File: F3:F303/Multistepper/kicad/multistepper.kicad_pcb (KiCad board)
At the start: 4 copper layers, 113.5 x 105.5 mm, 231 parts, among them J1 Prog, J10 Screw_Terminal_01x02, J11 LimS, J12 Stepper, J13 UART, J14 LimS, J15 Stepper, J16 LimS, J17 Stepper, J18 LimS, J19 Stepper, J2 Buttons/I2C, J20 LimS, J21 Stepper, J22 LimS, J23 Stepper, J24 LimS, J25 Stepper, J26 LimS, J27 Stepper, J3 Screen, J4 ADC2, J5 ADC1, J6 MOT_MUL, J7 GPO, J8 USB_B, J9 Screw_Terminal_01x03, Q1 B0505S, Q2 IRF9310, SW1 Reset, SW2 Boot, SW3 SW_DIP_x01, U1 STM32F303VDTx, U2 ISO1050DUB, U3 USBLC6-2SC6, U4 LM4050A(b)EX3-3.3, U5 LM2576-5.0, U6 LM1117-3.3, U7 74HC4051, Y1 NX5032GA-8MHz

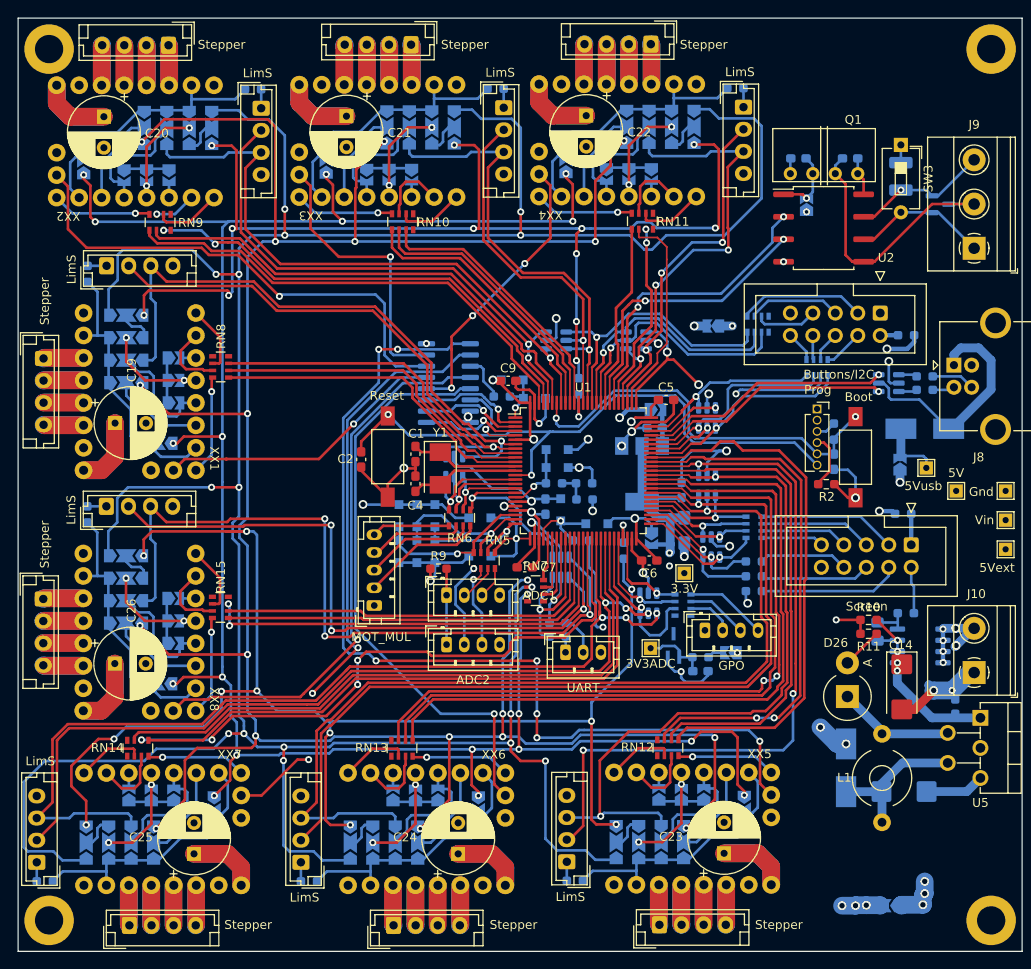
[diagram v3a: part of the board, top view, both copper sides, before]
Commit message: Multistepper PCB almost ready
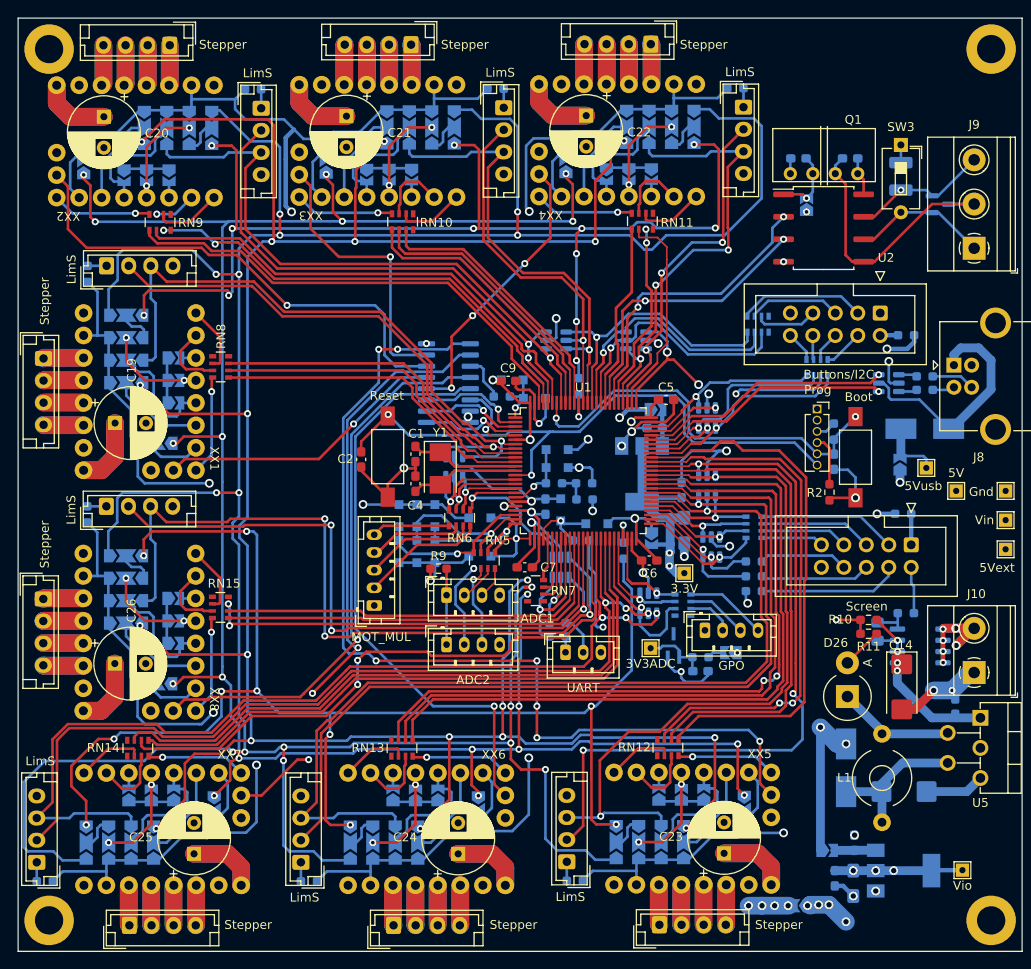
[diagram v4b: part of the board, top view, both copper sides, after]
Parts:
- added C27: 0.1, Capacitor_SMD:C_0603_1608Metric_Pad1.08x0.95mm_HandSolder, B.Cu at (150.0, 131.7)
- added C28: 47u 6V, Capacitor_Tantalum_SMD:CP_EIA-3216-18_Kemet-A_Pad1.58x1.35mm_HandSolder, B.Cu at (149.9, 136.3)
- added C29: 0.1, Capacitor_SMD:C_0603_1608Metric_Pad1.08x0.95mm_HandSolder, B.Cu at (147.8, 135.7)
- added TP8: Vio, TestPoint:TestPoint_THTPad_1.5x1.5mm_Drill0.7mm, F.Cu at (162.3, 134.8)
- added U8: LM1117-3.3, Package_TO_SOT_SMD:SOT-223-3_TabPin2, B.Cu at (155.6, 134.9)
- moved JP7 60.7 mm to (147.0, 132.6), turned to 0 degrees
- moved JP6 10.3 mm to (144.0, 138.8)
- moved R2 0.98 mm to (147.2, 92.1), turned to 90 degrees
- moved J15 0.14 mm to (72.6, 41.6)
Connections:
- JP10 pad 3: /Motors/Vio -> Vio
- JP11 pad 3: /Motors/Vio -> Vio
- JP12 pad 3: /Motors/Vio -> Vio
- JP16 pad 3: /Motors/Vio -> Vio
- JP18 pad 3: /Motors/Vio -> Vio
- JP19 pad 3: /Motors/Vio -> Vio
- JP20 pad 3: /Motors/Vio -> Vio
- JP24 pad 3: /Motors/Vio -> Vio
- JP26 pad 3: /Motors/Vio -> Vio
- JP27 pad 3: /Motors/Vio -> Vio
- JP28 pad 3: /Motors/Vio -> Vio
- JP32 pad 3: /Motors/Vio -> Vio
- JP34 pad 3: /Motors/Vio -> Vio
- JP35 pad 3: /Motors/Vio -> Vio
- JP36 pad 3: /Motors/Vio -> Vio
- JP40 pad 3: /Motors/Vio -> Vio
- JP42 pad 3: /Motors/Vio -> Vio
- JP43 pad 3: /Motors/Vio -> Vio
- JP44 pad 3: /Motors/Vio -> Vio
- JP48 pad 3: /Motors/Vio -> Vio
- JP50 pad 3: /Motors/Vio -> Vio
- JP51 pad 3: /Motors/Vio -> Vio
- JP52 pad 3: /Motors/Vio -> Vio
- JP56 pad 3: /Motors/Vio -> Vio
- JP58 pad 3: /Motors/Vio -> Vio
- JP59 pad 3: /Motors/Vio -> Vio
- JP60 pad 3: /Motors/Vio -> Vio
- JP64 pad 3: /Motors/Vio -> Vio
- JP66 pad 3: /Motors/Vio -> Vio
- JP67 pad 3: /Motors/Vio -> Vio
- JP68 pad 3: /Motors/Vio -> Vio
- JP7 pad 1: +3V3 -> +5V
- JP7 pad 2: /Motors/Vio -> Net-(C27-Pad1)
- JP8 pad 3: /Motors/Vio -> Vio
- R23 pad 1: /Motors/Vio -> Vio
- R26 pad 1: /Motors/Vio -> Vio
- R27 pad 1: /Motors/Vio -> Vio
- R28 pad 1: /Motors/Vio -> Vio
- R29 pad 1: /Motors/Vio -> Vio
- R30 pad 1: /Motors/Vio -> Vio
- R31 pad 1: /Motors/Vio -> Vio
- R32 pad 1: /Motors/Vio -> Vio
- U7 pad 16: /Motors/Vio -> Vio
- XX1 pad 10: /Motors/Vio -> Vio
- XX2 pad 10: /Motors/Vio -> Vio
- XX3 pad 10: /Motors/Vio -> Vio
- XX4 pad 10: /Motors/Vio -> Vio
- XX5 pad 10: /Motors/Vio -> Vio
- XX6 pad 10: /Motors/Vio -> Vio
- XX7 pad 10: /Motors/Vio -> Vio
- XX8 pad 10: /Motors/Vio -> Vio
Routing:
- net /Motors/Vio: track 587.4 -> 0.00 mm, vias 11 -> 0
- net Vio: track 0.00 -> 500.7 mm, vias 0 -> 11
- net +3V3: track 0.00 -> 81.1 mm
- net GND: track 1108.3 -> 1142.8 mm, vias 21 -> 24
- net Vdrive: track 111.2 -> 139.9 mm, vias 7 -> 8
- net Net-(J10-Pad2): track 20.0 -> 39.2 mm
- net +5V: track 177.6 -> 188.0 mm
- net /Motors/Vm: track 502.7 -> 494.0 mm, vias 3 -> 4
- net Net-(C27-Pad1): track 0.00 -> 4.62 mm
- net ADC4: track 47.1 -> 45.4 mm
- net /MCU base/A1: track 19.1 -> 17.6 mm
- net M4_L0: track 83.2 -> 84.6 mm
- net /Motors/MOSI: track 239.2 -> 238.0 mm
- net /MCU base/Diagn: track 6.80 -> 5.79 mm
- net /Motors/DIAG1: track 57.2 -> 56.3 mm
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- added copper zone on In2.Cu, net MCU3v3
